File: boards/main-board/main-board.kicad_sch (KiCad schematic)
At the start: 1 part

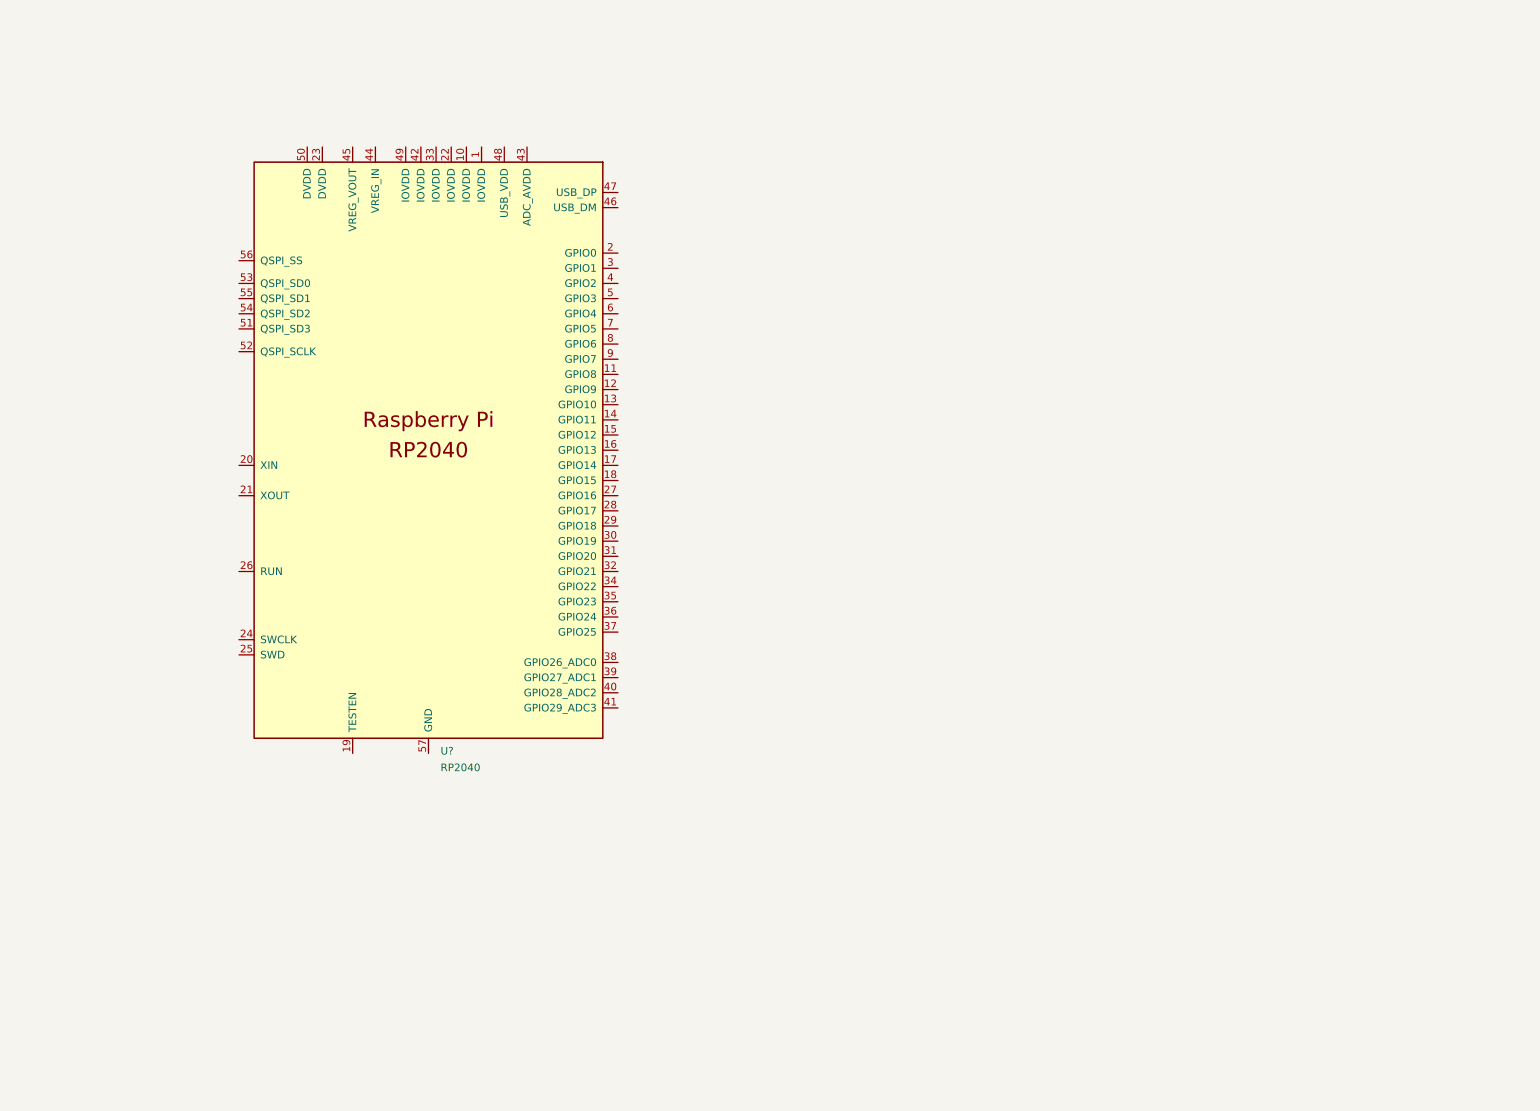
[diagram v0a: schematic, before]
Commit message: Added basic RP2040 schematics
Signed-off-by: Computroniks <mnickson@sidingsmedia.com>
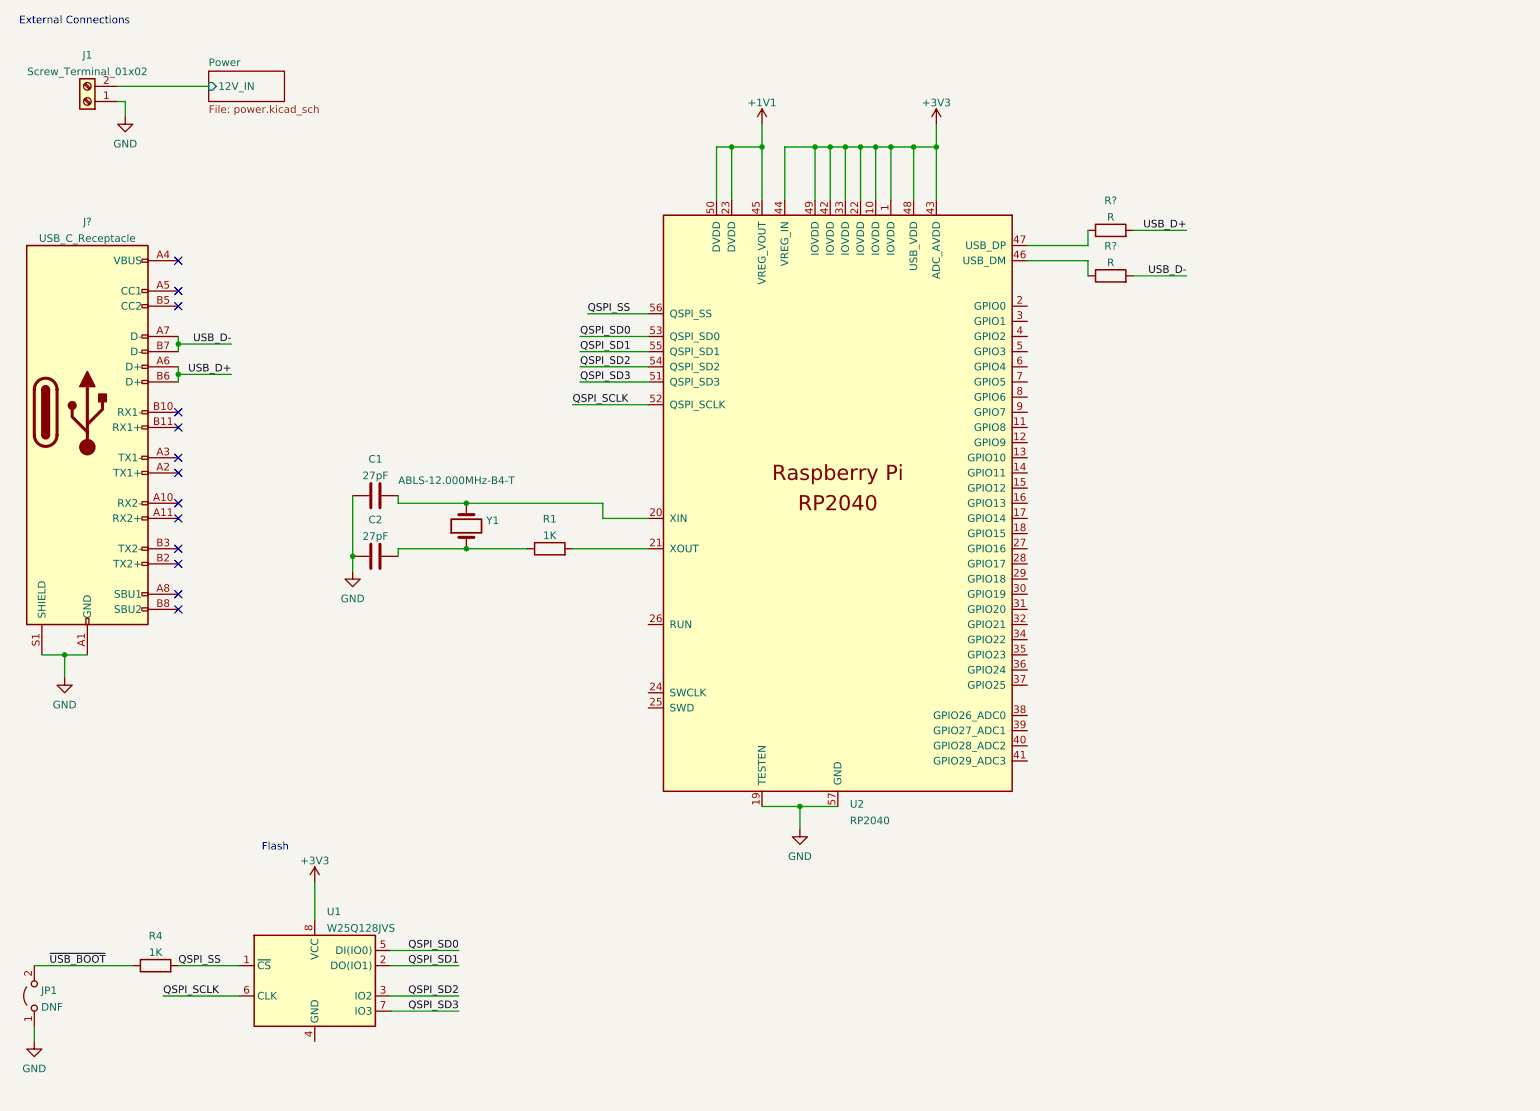
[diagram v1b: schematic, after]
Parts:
- added C1, C2: 27pF, symbol Device:C
- added J1: Screw_Terminal_01x02, symbol Connector:Screw_Terminal_01x02
- added J?: USB_C_Receptacle, symbol Connector:USB_C_Receptacle
- added JP1: DNF, symbol Jumper:Jumper_2_Open
- added R1, R4: 1K, symbol Device:R
- added R? (x2): R, symbol Device:R
- added U1: W25Q128JVS, Package_SO:SOIC-8_5.23x5.23mm_P1.27mm, symbol Memory_Flash:W25Q128JVS
- added Y1: ABLS-12.000MHz-B4-T, symbol Device:Crystal
- gave numbers to parts that had none: 1
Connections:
- net +3V3: now reaches U2.1 (IOVDD)
- net +3V3: now also U2.10 (IOVDD), U2.22 (IOVDD), U2.33 (IOVDD), U2.42 (IOVDD), U2.43 (ADC_AVDD), U2.44 (VREG_IN), U2.48 (USB_VDD), U2.49 (IOVDD), U1.8 (VCC)
- net GND: now reaches U2.19 (TESTEN)
- net GND: now also U2.57 (GND), C1.1, C2.1, J1.1 (Pin_1), J?.A1 (GND), J?.A12 (GND), J?.B1 (GND), J?.B12 (GND), J?.S1 (SHIELD), JP1.1 (A)
- net at U2.20 (XIN): now also C1.2, Y1.2
- net at U2.21 (XOUT): now also R1.2
- net +1V1: now reaches U2.23 (DVDD)
- net +1V1: now also U2.45 (VREG_VOUT), U2.50 (DVDD)
- net at U2.46 (USB_DM): now also R?.1
- net at U2.47 (USB_DP): now also R?.1
- net QSPI_SD3: now reaches U2.51 (QSPI_SD3)
- net QSPI_SD3: now also U1.7 (IO3)
- net QSPI_SCLK: now reaches U2.52 (QSPI_SCLK)
- net QSPI_SCLK: now also U1.6 (CLK)
- net QSPI_SD0: now reaches U2.53 (QSPI_SD0)
- net QSPI_SD0: now also U1.5 (DI(IO0))
- net QSPI_SD2: now reaches U2.54 (QSPI_SD2)
- net QSPI_SD2: now also U1.3 (IO2)
- net QSPI_SD1: now reaches U2.55 (QSPI_SD1)
- net QSPI_SD1: now also U1.2 (DO(IO1))
- net QSPI_SS: now reaches U2.56 (QSPI_SS)
- net QSPI_SS: now also R4.2, U1.1 (~{CS})
- new net: C2.2, R1.1, Y1.1
- new net: J?.A4 (VBUS), J?.A9 (VBUS), J?.B4 (VBUS), J?.B9 (VBUS)
- new net Power/12V_IN: J1.2 (Pin_2)
- new net USB_D+: J?.A6 (D+), J?.B6 (D+), R?.2
- new net USB_D-: J?.A7 (D-), J?.B7 (D-), R?.2
- new net ~{USB_BOOT}: JP1.2 (B), R4.1
- no-connect marks 0 -> 13
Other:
- added sheet Power (power.kicad_sch)
- note added: "External Connections"
- note added: "Flash"
- moved on the sheet: U2

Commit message: Version 1.1.0 of main control board schematic
Signed-off-by: Computroniks <mnickson@sidingsmedia.com>
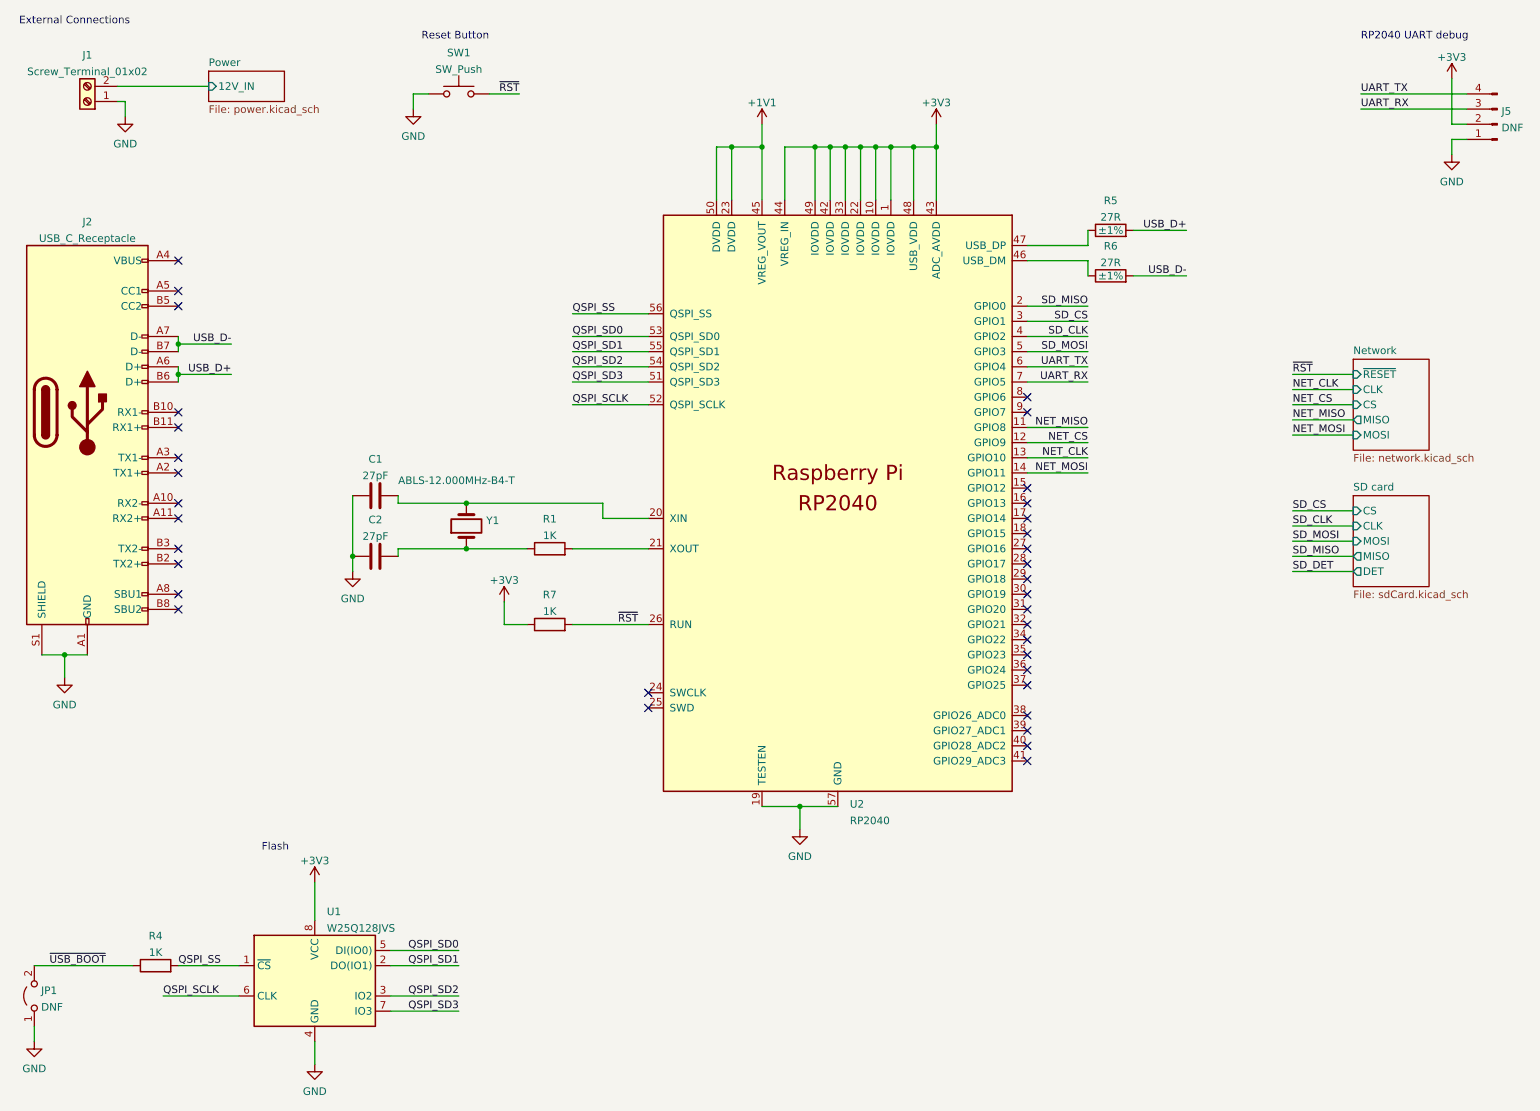
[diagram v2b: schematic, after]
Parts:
- added J5: DNF, Connector_PinHeader_2.54mm:PinHeader_1x04_P2.54mm_Vertical, symbol Connector:Conn_01x04_Male
- added R7: 1K, Resistor_SMD:R_0805_2012Metric, symbol Device:R
- added SW1: SW_Push, Button_Switch_SMD:SW_Push_1P1T_NO_6x6mm_H9.5mm, symbol Switch:SW_Push
- C1, C2: footprint (none) -> Capacitor_SMD:C_0805_2012Metric
- J1: footprint (none) -> TerminalBlock:TerminalBlock_Altech_AK300-2_P5.00mm
- J2: renamed from J?; footprint (none) -> Connector_USB:USB_C_Receptacle_Amphenol_12401610E4-2A
- JP1: footprint (none) -> Jumper:SolderJumper-2_P1.3mm_Open_Pad1.0x1.5mm
- R1, R4: footprint (none) -> Resistor_SMD:R_0805_2012Metric
- R5, R6: renamed from R?; value R -> 27R; footprint (none) -> Resistor_SMD:R_0805_2012Metric; Tolerance (none) -> ±1%
- Y1: footprint (none) -> Crystal:Crystal_SMD_HC49-SD
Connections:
- net +3V3: now also J5.2 (Pin_2), R7.1
- net GND: now also U1.4 (GND), J5.1 (Pin_1), SW1.1
- net NET_MISO: now reaches U2.11 (GPIO8)
- net NET_CS: now reaches U2.12 (GPIO9)
- net NET_CLK: now reaches U2.13 (GPIO10)
- net NET_MOSI: now reaches U2.14 (GPIO11)
- net SD_MISO: now reaches U2.2 (GPIO0)
- net ~{RST}: now reaches U2.26 (RUN)
- net ~{RST}: now also R7.2, SW1.2
- net SD_CS: now reaches U2.3 (GPIO1)
- net SD_CLK: now reaches U2.4 (GPIO2)
- net SD_MOSI: now reaches U2.5 (GPIO3)
- net UART_TX: now reaches U2.6 (GPIO4)
- net UART_TX: now also J5.4 (Pin_4)
- net UART_RX: now reaches U2.7 (GPIO5)
- net UART_RX: now also J5.3 (Pin_3)
- no-connect marks 13 -> 35
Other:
- added sheet Network (network.kicad_sch)
- added sheet SD card (sdCard.kicad_sch)
- note added: "RP2040 UART debug"
- note added: "Reset Button"

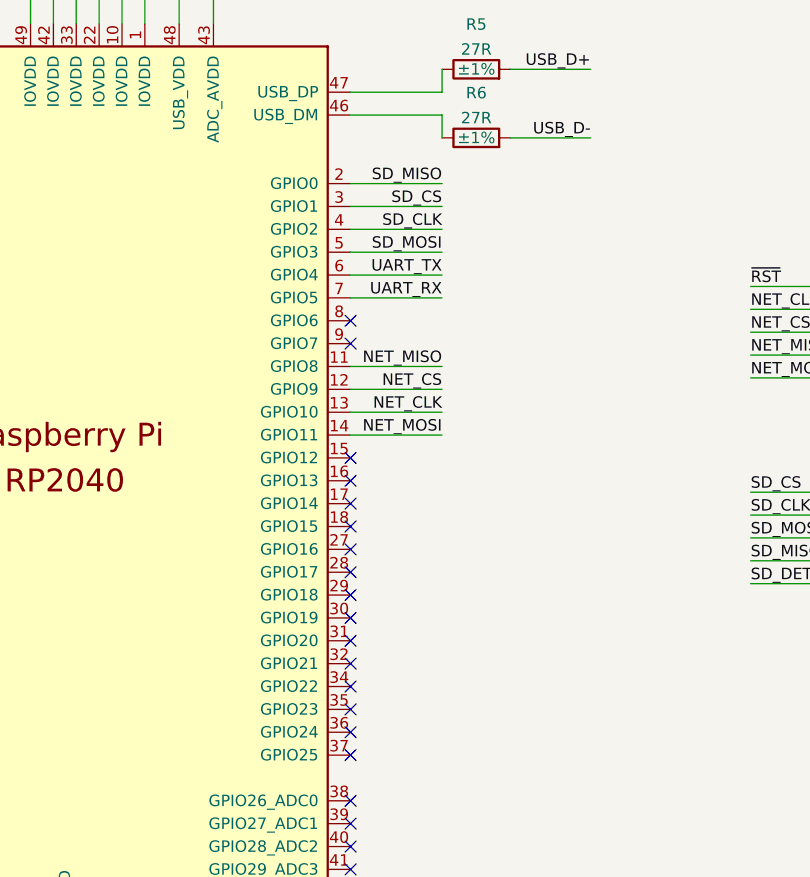
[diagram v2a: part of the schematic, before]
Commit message: Moved SPI connections + increment version
Signed-off-by: Computroniks <mnickson@sidingsmedia.com>
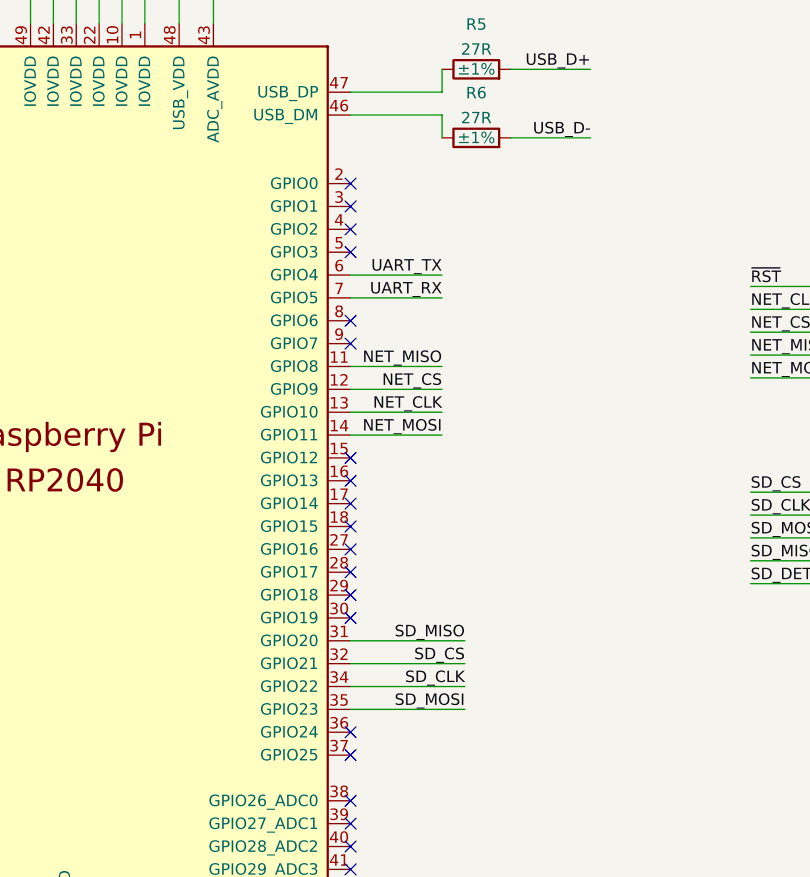
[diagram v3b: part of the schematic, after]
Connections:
- net SD_CLK: now also U2.34 (GPIO22); no longer U2.4 (GPIO2)
- net SD_CS: now also U2.32 (GPIO21); no longer U2.3 (GPIO1)
- net SD_MISO: now also U2.31 (GPIO20); no longer U2.2 (GPIO0)
- net SD_MOSI: now also U2.35 (GPIO23); no longer U2.5 (GPIO3)
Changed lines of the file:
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@@
     (title "Main Board")
     (date "2022-03-18")
-    (rev "V1.1.0")
+    (rev "V1.1.1")
     (company "Matthew Nickson")
     (comment 1 "Licence: CC-BY-SA-4.0")
@@
   (no_connect (at 185.42 127))
   (no_connect (at 185.42 124.46))
-  (no_connect (at 185.42 121.92))
-  (no_connect (at 185.42 119.38))
-  (no_connect (at 185.42 116.84))
-  (no_connect (at 185.42 114.3))
   (no_connect (at 185.42 111.76))
+  (no_connect (at 185.42 63.5))
+  (no_connect (at 185.42 66.04))
+  (no_connect (at 185.42 68.58))
+  (no_connect (at 185.42 71.12))
   (no_connect (at 43.18 55.88))
   (no_connect (at 43.18 81.28))
@@
     (stroke (width 0) (type default) (color 0 0 0 0))
   )
-  (wire (pts (xy 185.42 68.58) (xy 195.58 68.58))
-    (stroke (width 0) (type default) (color 0 0 0 0))
-  )
   (wire (pts (xy 229.87 107.95) (xy 240.03 107.95))
     (stroke (width 0) (type default) (color 0 0 0 0))
@@
     (stroke (width 0) (type default) (color 0 0 0 0))
   )
+  (wire (pts (xy 185.42 119.38) (xy 198.12 119.38))
+    (stroke (width 0) (type default) (color 0 0 0 0))
+  )
   (wire (pts (xy 66.04 186.69) (xy 66.04 190.5))
     (stroke (width 0) (type default) (color 0 0 0 0))
@@
     (stroke (width 0) (type default) (color 0 0 0 0))
   )
-  (wire (pts (xy 185.42 71.12) (xy 195.58 71.12))
-    (stroke (width 0) (type default) (color 0 0 0 0))
-  )
   (wire (pts (xy 140.97 147.32) (xy 147.32 147.32))
     (stroke (width 0) (type default) (color 0 0 0 0))
@@
     (stroke (width 0) (type default) (color 0 0 0 0))
   )
+  (wire (pts (xy 185.42 121.92) (xy 198.12 121.92))
+    (stroke (width 0) (type default) (color 0 0 0 0))
+  )
   (wire (pts (xy 166.37 36.83) (xy 170.18 36.83))
     (stroke (width 0) (type default) (color 0 0 0 0))
@@
     (stroke (width 0) (type default) (color 0 0 0 0))
   )
+  (wire (pts (xy 185.42 116.84) (xy 198.12 116.84))
+    (stroke (width 0) (type default) (color 0 0 0 0))
+  )
   (wire (pts (xy 109.22 80.01) (xy 121.92 80.01))
     (stroke (width 0) (type default) (color 0 0 0 0))
@@
     (stroke (width 0) (type default) (color 0 0 0 0))
   )
-  (wire (pts (xy 185.42 66.04) (xy 195.58 66.04))
+  (wire (pts (xy 185.42 114.3) (xy 198.12 114.3))
     (stroke (width 0) (type default) (color 0 0 0 0))
   )
@@
     (stroke (width 0) (type default) (color 0 0 0 0))
   )
-  (wire (pts (xy 185.42 63.5) (xy 195.58 63.5))
-    (stroke (width 0) (type default) (color 0 0 0 0))
-  )
   (wire (pts (xy 157.48 36.83) (xy 160.02 36.83))
     (stroke (width 0) (type default) (color 0 0 0 0))
@@
     (effects (font (size 1.27 1.27)) (justify right bottom))
   )
-  (label "SD_CLK" (at 195.58 68.58 180)
-    (effects (font (size 1.27 1.27)) (justify right bottom))
-  )
   (label "QSPI_SD3" (at 90.17 181.61 180)
     (effects (font (size 1.27 1.27)) (justify right bottom))
@@
     (effects (font (size 1.27 1.27)) (justify left bottom))
   )
+  (label "SD_MOSI" (at 198.12 121.92 180)
+    (effects (font (size 1.27 1.27)) (justify right bottom))
+  )
   (label "NET_CS" (at 195.58 86.36 180)
     (effects (font (size 1.27 1.27)) (justify right bottom))
   )
-  (label "SD_MOSI" (at 195.58 71.12 180)
-    (effects (font (size 1.27 1.27)) (justify right bottom))
-  )
   (label "~{RST}" (at 116.84 116.84 0)
     (effects (font (size 1.27 1.27)) (justify left bottom))
@@
     (effects (font (size 1.27 1.27)) (justify left bottom))
   )
+  (label "SD_CLK" (at 198.12 119.38 180)
+    (effects (font (size 1.27 1.27)) (justify right bottom))
+  )
   (label "QSPI_SD0" (at 90.17 171.45 180)
     (effects (font (size 1.27 1.27)) (justify right bottom))
@@
     (effects (font (size 1.27 1.27)) (justify left bottom))
   )
-  (label "SD_MISO" (at 195.58 63.5 180)
-    (effects (font (size 1.27 1.27)) (justify right bottom))
-  )
   (label "UART_RX" (at 241.3 30.48 0)
     (effects (font (size 1.27 1.27)) (justify left bottom))
@@
     (effects (font (size 1.27 1.27)) (justify left bottom))
   )
-  (label "SD_CS" (at 195.58 66.04 180)
+  (label "SD_MISO" (at 198.12 114.3 180)
     (effects (font (size 1.27 1.27)) (justify right bottom))
   )
@@
     (effects (font (size 1.27 1.27)) (justify left bottom))
   )
+  (label "SD_CS" (at 198.12 116.84 180)
+    (effects (font (size 1.27 1.27)) (justify right bottom))
+  )
   (label "NET_MISO" (at 195.58 83.82 180)
